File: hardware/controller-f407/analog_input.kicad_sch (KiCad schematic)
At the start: 31 parts, among them J20 EL_POT

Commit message: edits for clarity after Grok created the sheets...still more work to do.
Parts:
- renumbered C201 to C17, C211 to C18, C221 to C19, C231 to C20, D201 to D14, D202 to D15, D211 to D16, D212 to D17, D221 to D18, D260 to D19, D222 to D20, D231 to D21, D261 to D22, D232 to D23, D250 to D24, D251 to D25, J20 to J5, R201 to R31, R202 to R32, R203 to R33, R211 to R34, R212 to R35, R213 to R36, R221 to R37, R222 to R38, R223 to R39, R231 to R40, R232 to R41, R233 to R42, R250 to R43, R251 to R44
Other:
- moved on the sheet: C17, C18, C19, C20, D14, D15, D16, D17, D18, D19, D20, D21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

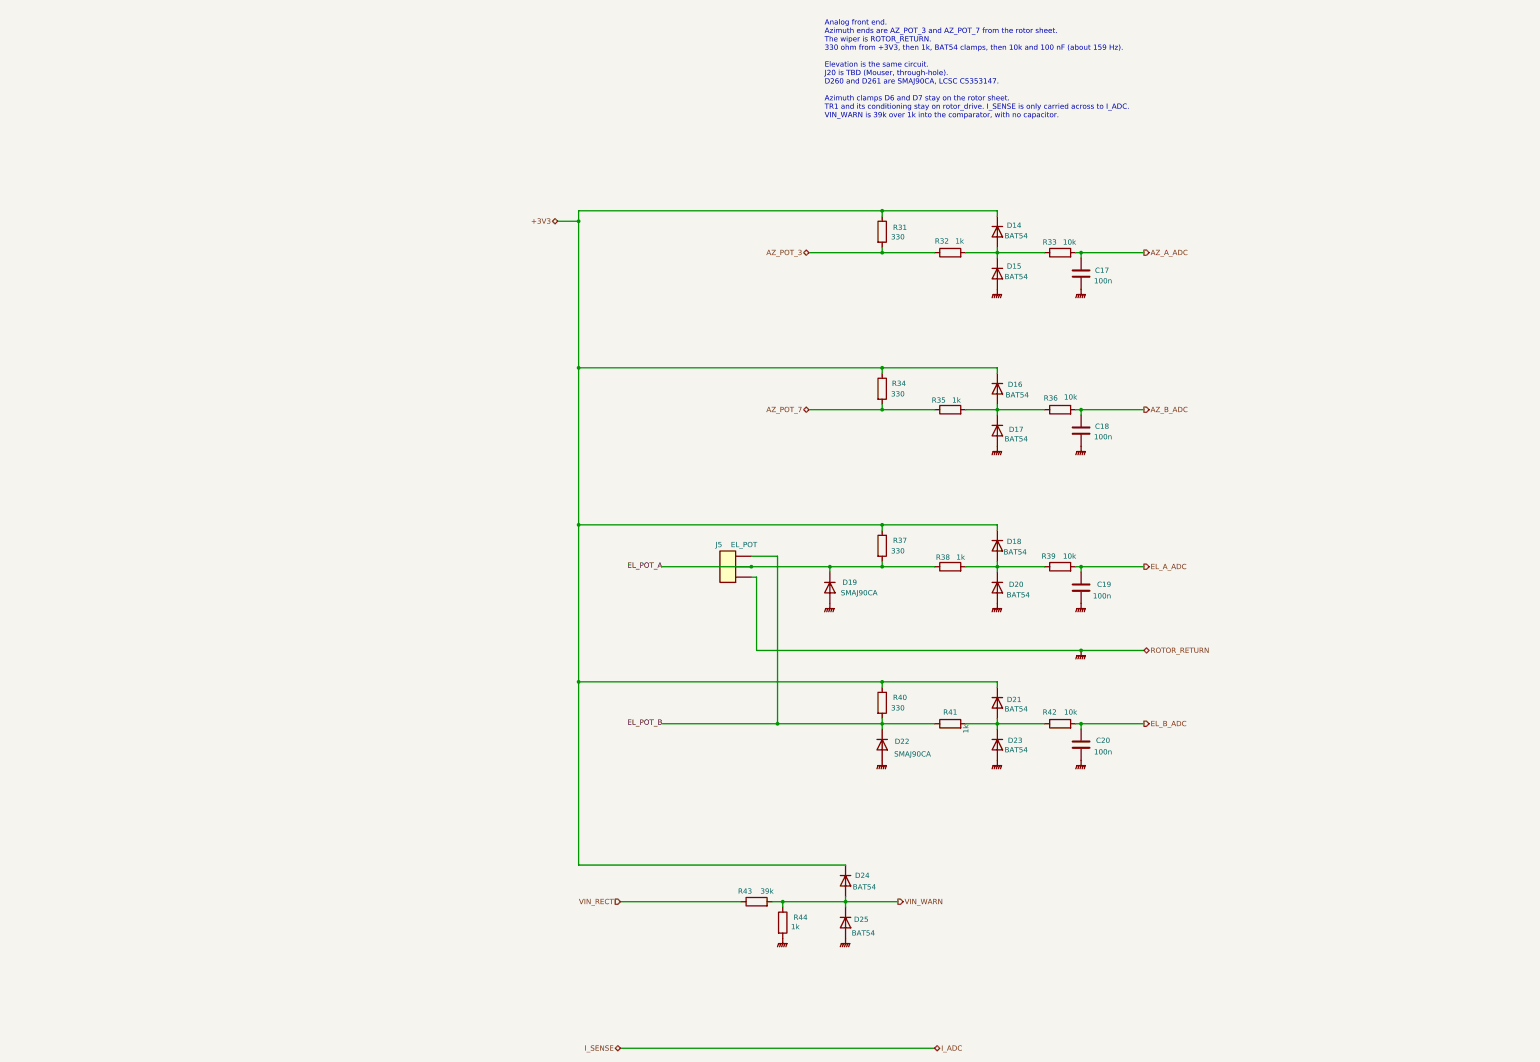
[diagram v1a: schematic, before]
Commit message: Add a 60 Hz twin-T on each pot sense line.
The shared rotor return can carry several volts of 60 Hz, so each sense line is 1k, then 121k/60.4k/22n twin-T, then the existing 10k/100nF, then the BAT54 clamps. Elevation J5 is a 3-pin connector valued ELEVATION ROTOR. Owner text on the analog sheet is recorded and not moved.

Co-authored-by: Jeffrey Millar <wa1hco@users.noreply.github.com>
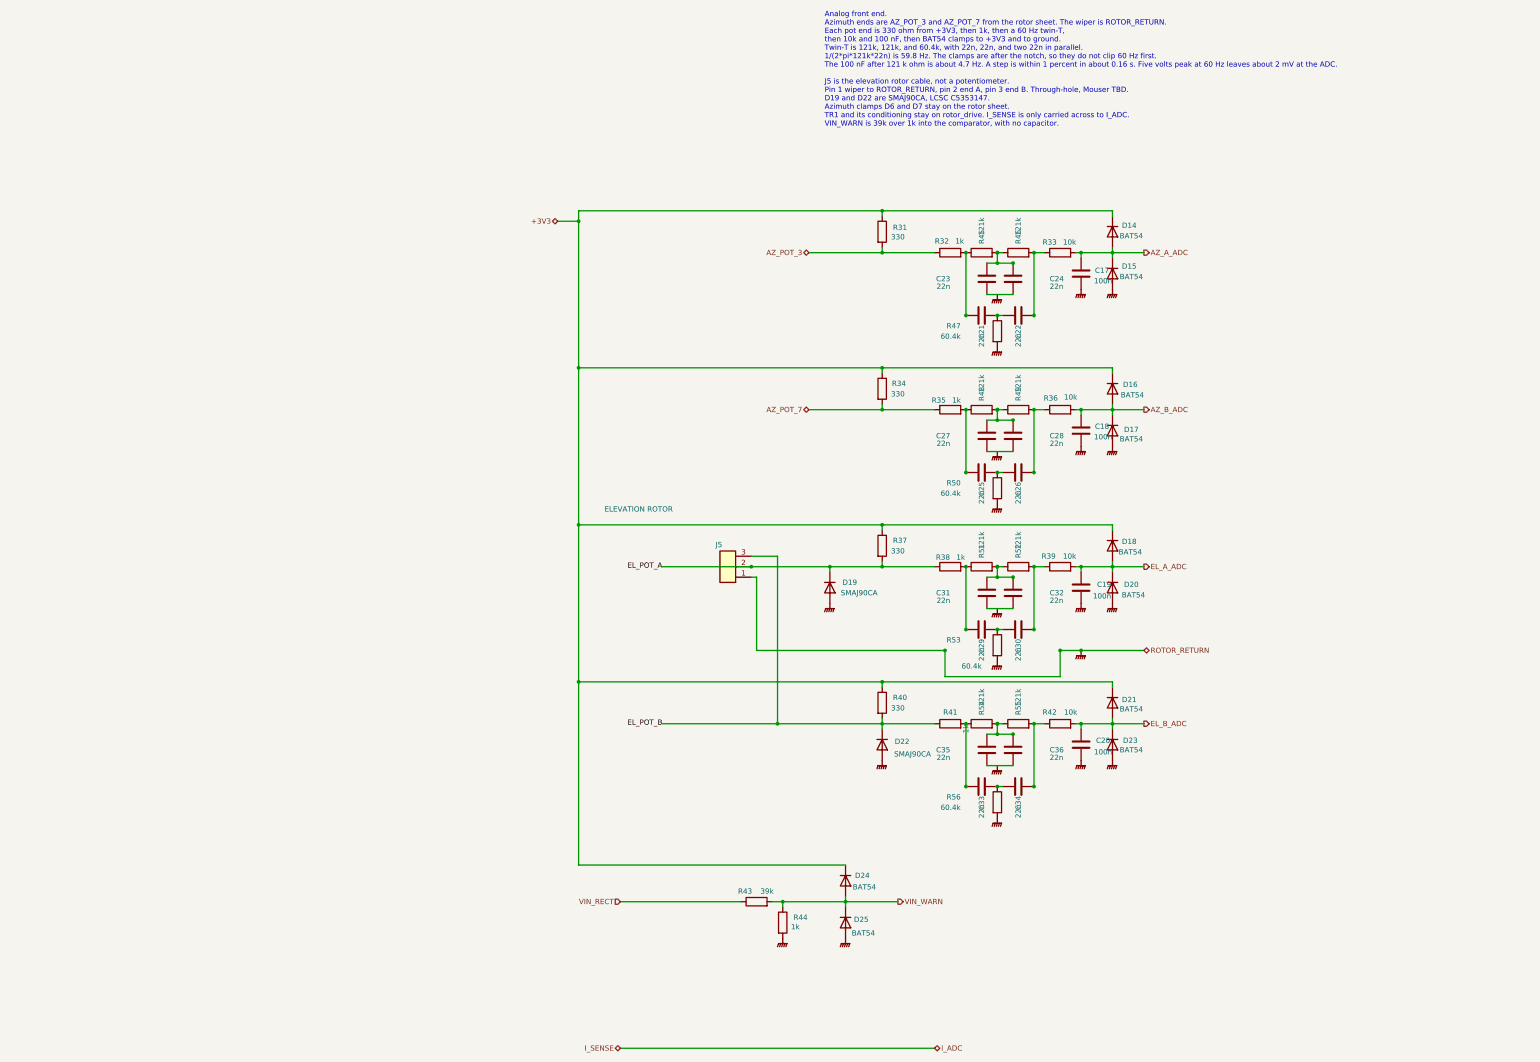
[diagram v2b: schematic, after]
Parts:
- added C21, C22, C23, C24, C25, C26, C27, C28, C29, C30, C31, C32, C33, C34, C35, C36: 22n, Capacitor_SMD:C_0805_2012Metric, symbol Device:C
- added R45, R46, R48, R49, R51, R52, R54, R55: 121k, Resistor_SMD:R_0603_1608Metric, symbol Device:R
- added R47, R50, R53, R56: 60.4k, Resistor_SMD:R_0603_1608Metric, symbol Device:R
- J5: value EL_POT -> ELEVATION ROTOR
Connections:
- net AZ_A_ADC: now also D14.2 (A), D15.1 (K)
- net AZ_B_ADC: now also D16.2 (A), D17.1 (K)
- net EL_A_ADC: now also D18.2 (A), D20.1 (K)
- net EL_B_ADC: now also D21.2 (A), D23.1 (K)
- net GNDPWR: now also C23.2, C24.2, C27.2, C28.2, C31.2, C32.2, C35.2, C36.2, R47.2, R50.2, R53.2, R56.2
- new net: C29.2, C30.1, R53.1
- new net: C30.2, R39.1, R52.2
- new net: C35.1, C36.1, R54.2, R55.1
- new net: C31.1, C32.1, R51.2, R52.1
- new net: C27.1, C28.1, R48.2, R49.1
- new net: C26.2, R36.1, R49.2
- new net: C25.1, R35.2, R48.1
- new net: C25.2, C26.1, R50.1
- new net: C33.2, C34.1, R56.1
- new net: C23.1, C24.1, R45.2, R46.1
- new net: C22.2, R33.1, R46.2
- new net: C29.1, R38.2, R51.1
- new net: C33.1, R41.2, R54.1
- new net: C34.2, R42.1, R55.2
- new net: C21.2, C22.1, R47.1
- new net: C21.1, R32.2, R45.1
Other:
- note added: "Analog front end. Azimuth ends are AZ_POT_3 and AZ_POT_7 from the rotor sheet. The wiper is ROTOR_RETURN. Each pot end is 330 ohm from +3V3, then 1k, then a 60 Hz twin-T, then 10k and 100 nF, then BAT54 clamps to +3V3 and to ground. Twin-T is 121k, 121k, and 60.4k, with 22n, 22n, and two 22n in parallel. 1/(2*pi*121k*22n) is 59.8 Hz. The clamps are after the notch, so they do not clip 60 Hz first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"
- note removed: "Analog front end. Azimuth ends are AZ_POT_3 and AZ_POT_7 from the rotor sheet. The wiper is ROTOR_RETURN. 330 ohm from +3V3, then 1k, BAT54 clamps, then 10k and 100 nF (about 159 Hz). Elevation is the same circuit. J20 is TBD (Mouser, through-hole). D260 and D261 are SMAJ90CA, LCSC C5353147. Azimuth clamps D6 and D7 stay on the rotor sheet. TR1 and its conditioning stay on rotor_drive. I_SENSE is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"
- moved on the sheet: D14, D15, D16, D17, D18, D20, D21, D23
